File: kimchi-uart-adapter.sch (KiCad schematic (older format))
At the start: 29 parts, among them IC1 MIC5504-1.8YM5-TR, J1 TYPE-C-31-M-12, J2 Conn_01x02, J3 SM06B-SRSS-TB(LF)(SN), U1 TPD2E001DRSR, U2 FT230XS

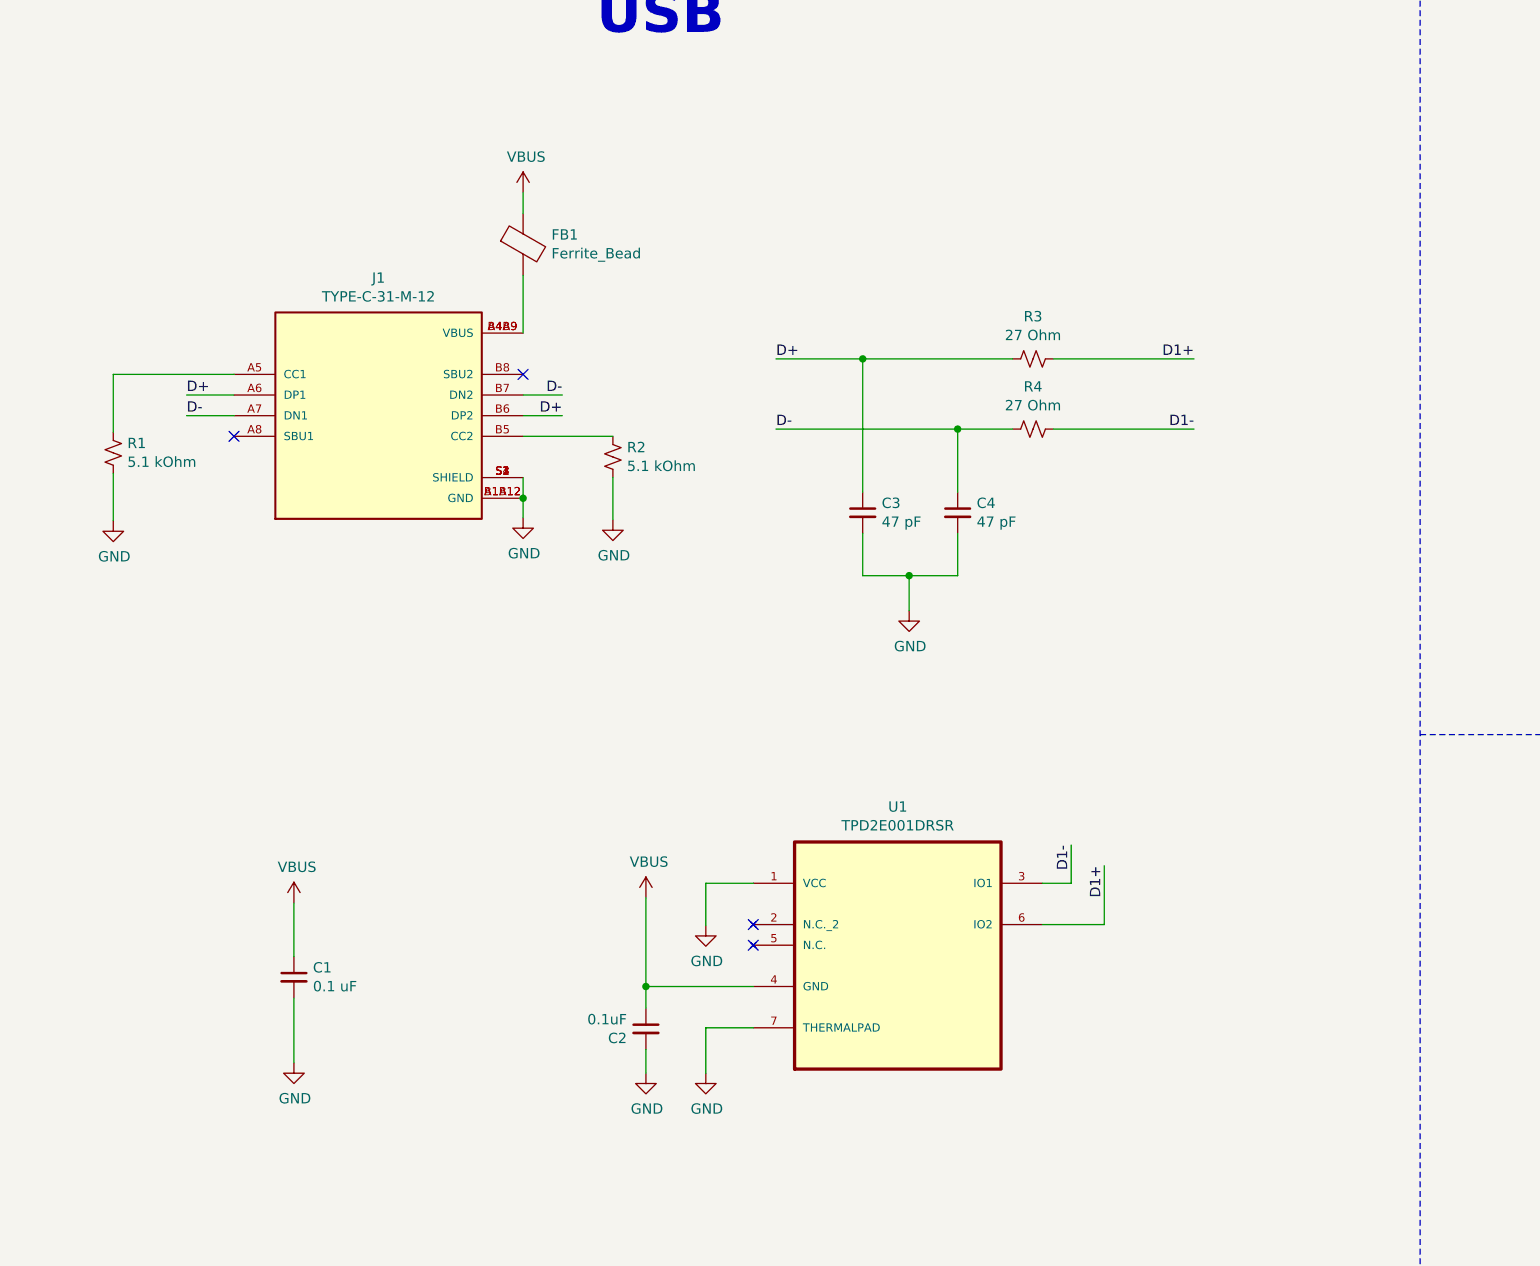
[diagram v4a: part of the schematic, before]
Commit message: Completed routing of uart lid
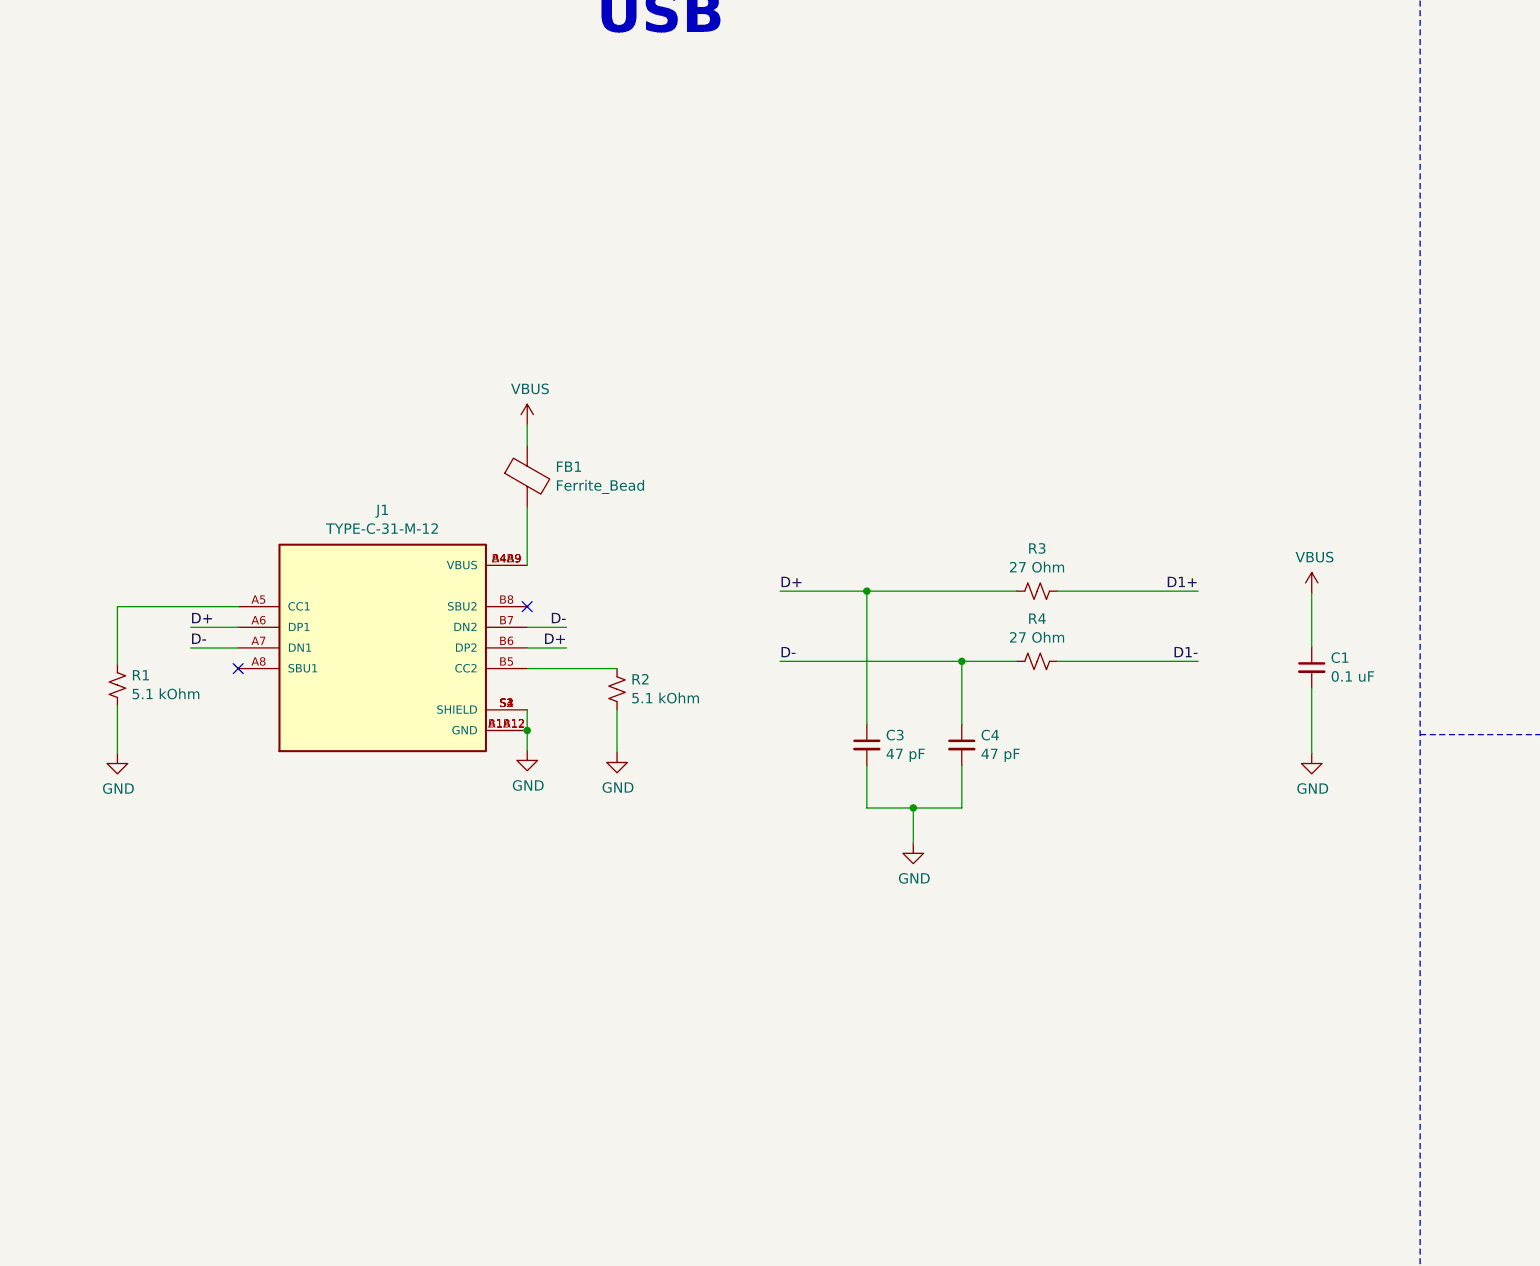
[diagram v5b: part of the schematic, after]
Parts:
- removed C2: 0.1uF, Capacitor_SMD:C_0603_1608Metric, symbol Device:C_Small
- removed U1: TPD2E001DRSR, footprints:SON95P315X315X80-7N, symbol TPD2E001DRSR:TPD2E001DRSR
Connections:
- no-connect marks 8 -> 6
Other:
- moved on the sheet: C1, C3, C4, FB1, J1, R1, R2, R3, R4
